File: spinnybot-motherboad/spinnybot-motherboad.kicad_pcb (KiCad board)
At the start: 2 copper layers, 76.2 x 76 mm, 55 parts, among them J1 +12V, J11 POWER SW2, J12 LEDSTRIP3, J13 LEDSTRIP2, J14 LEDSTRIP3, J2 LEDSTRIP1, J3 LEDSTRIP1, J4 LEDSTRIP2, J5 GND, J6 MOTOR2, J7 MOTOR3, J8 MOTOR1, J9 POWER SW1, Q1 SISA96DN, Q2 SISA96DN, Q3 BC846, Q4 Q_NMOS_DGS, U1 LM1117-3.3, U2 XBP9B-DMWTB002, U4 ICM-20649, U5 ESP32-DEVKITC-32D, U6 SN74AHCT541DW, U7 SN74AHCT541DW

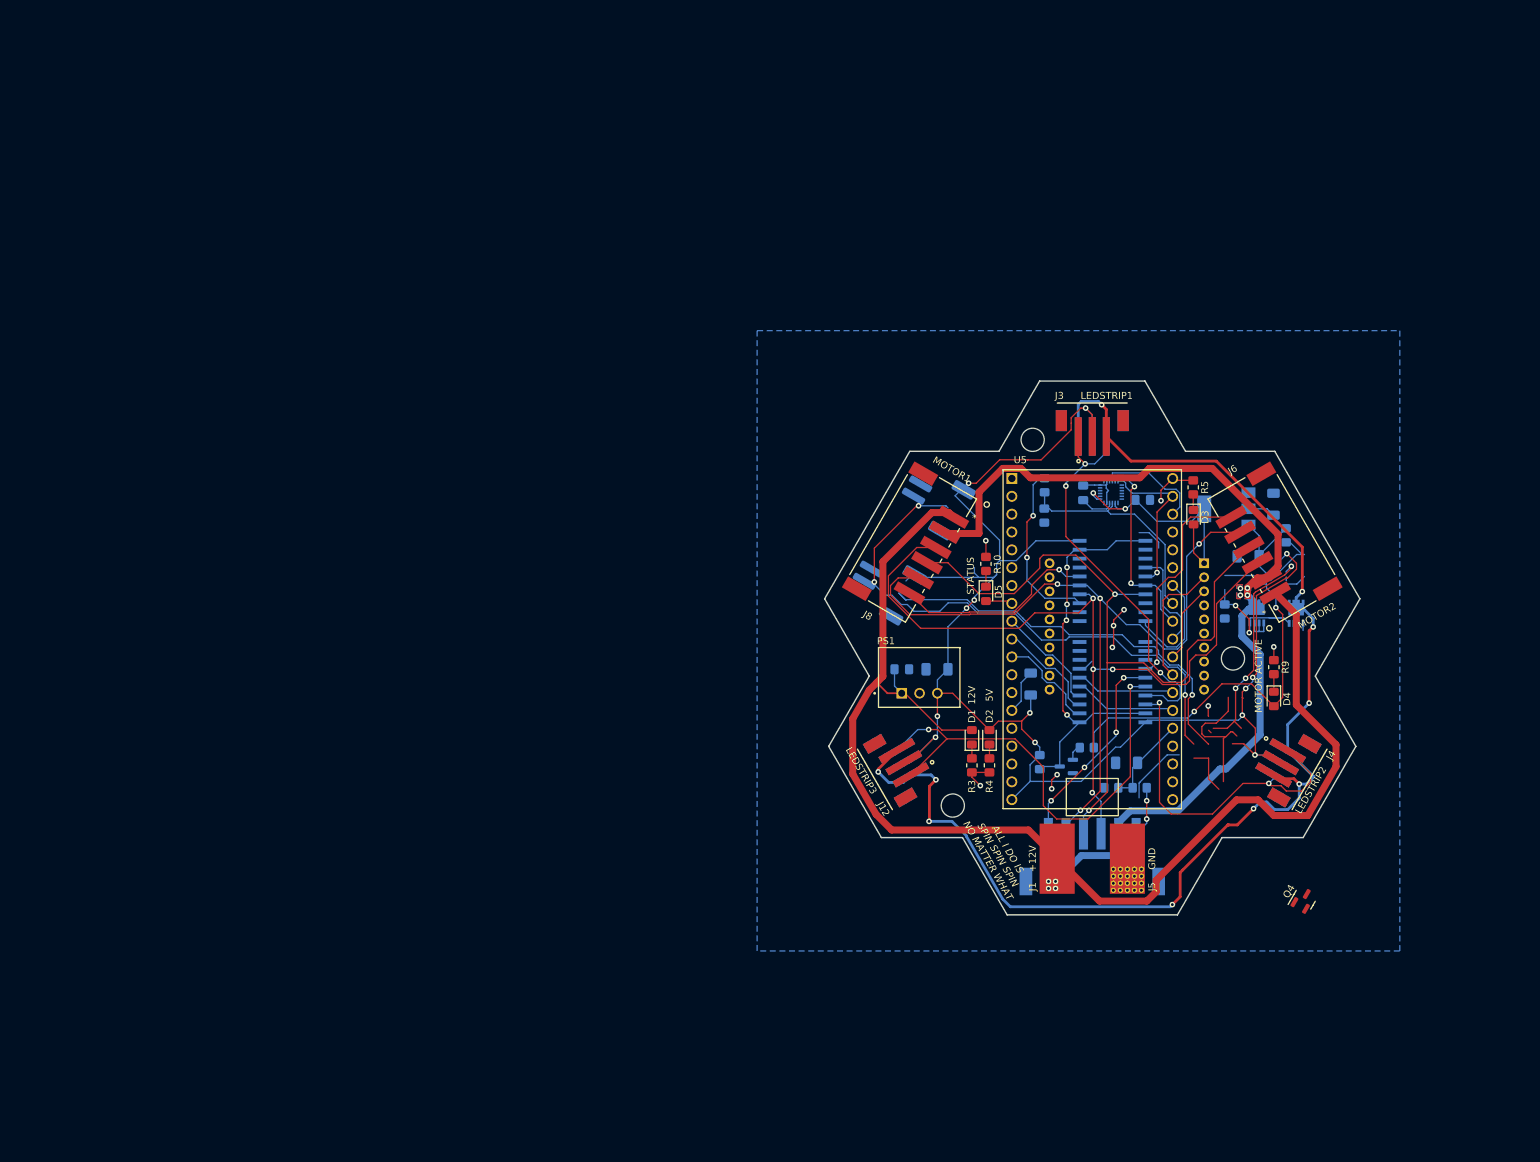
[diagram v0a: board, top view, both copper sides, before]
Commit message: Started board layout
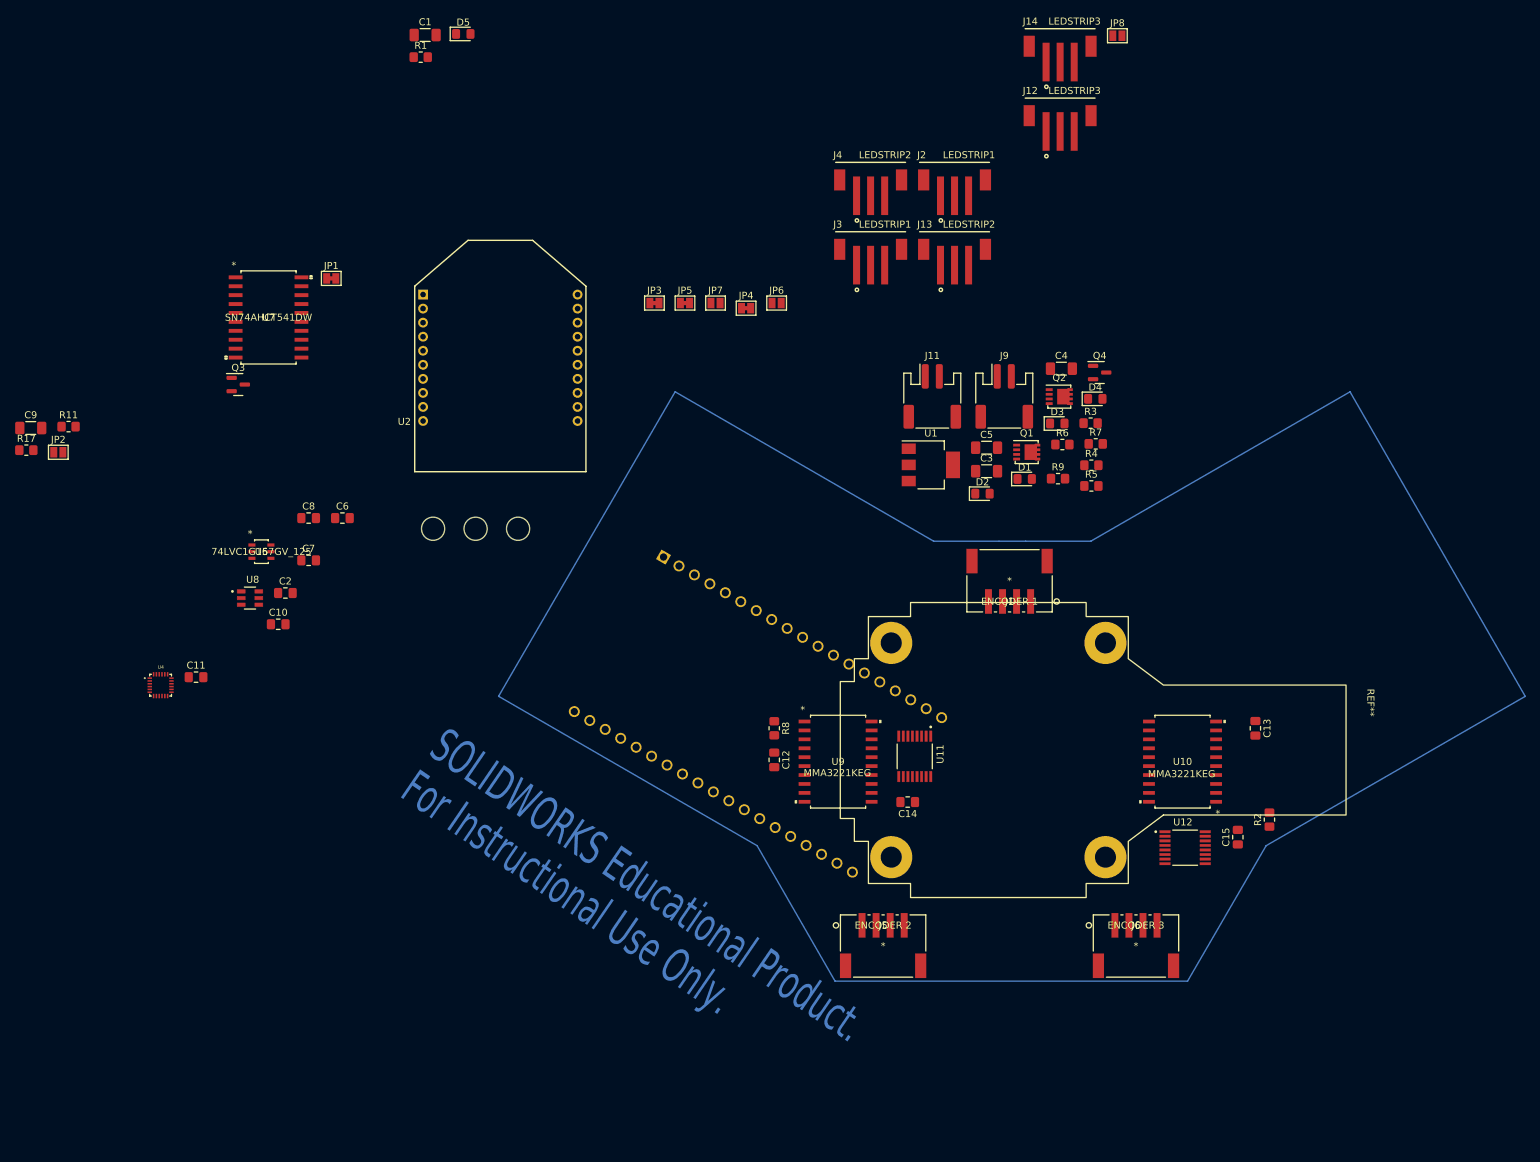
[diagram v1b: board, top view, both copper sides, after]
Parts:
- removed #LOGO1: LOGO, robologo-shenzen-25mm:F.SilkS_g1611
- removed #LOGO2: nofcc, robologo-shenzen-25mm:nofcc
- removed J7: MOTOR3, S6B-XH-SM4-TB:S6B-XH-SM4-TBLFSN
- removed J8: MOTOR1, S6B-XH-SM4-TB:S6B-XH-SM4-TBLFSN
- removed PS1: R-78E5.0-1.0, R-78E5:CONV_R-78E5.0-1.0
- removed R10: 130, Resistor_SMD:R_0805_2012Metric_Pad1.20x1.40mm_HandSolder
- removed R12: 1K, Resistor_SMD:R_0805_2012Metric_Pad1.20x1.40mm_HandSolder
- removed R13: 2K, Resistor_SMD:R_0805_2012Metric_Pad1.20x1.40mm_HandSolder
- added C10: 0.1u, Capacitor_SMD:C_0805_2012Metric_Pad1.18x1.45mm_HandSolder, F.Cu at (56.9, 99.2)
- added C11: 0.1u, Capacitor_SMD:C_0805_2012Metric_Pad1.18x1.45mm_HandSolder, F.Cu at (45.2, 106.7)
- added C12: 0.1u, Capacitor_SMD:C_0805_2012Metric_Pad1.18x1.45mm_HandSolder, F.Cu at (127.5, 118.5)
- added C13: 0.1u, Capacitor_SMD:C_0805_2012Metric_Pad1.18x1.45mm_HandSolder, F.Cu at (196.0, 114.0)
- added C14: 0.1u, Capacitor_SMD:C_0805_2012Metric_Pad1.18x1.45mm_HandSolder, F.Cu at (146.5, 124.5)
- added C15: 0.1u, Capacitor_SMD:C_0805_2012Metric_Pad1.18x1.45mm_HandSolder, F.Cu at (193.5, 129.5)
- added C6: 0.1u, Capacitor_SMD:C_0805_2012Metric_Pad1.18x1.45mm_HandSolder, F.Cu at (66.0, 84.1)
- added JP1: SolderJumper_2_Bridged, Jumper:SolderJumper-2_P1.3mm_Bridged_Pad1.0x1.5mm, F.Cu at (64.4, 50.0)
- added JP2: SolderJumper_2_Open, Jumper:SolderJumper-2_P1.3mm_Open_Pad1.0x1.5mm, F.Cu at (25.6, 74.7)
- added JP3: SolderJumper_2_Bridged, Jumper:SolderJumper-2_P1.3mm_Bridged_Pad1.0x1.5mm, F.Cu at (110.4, 53.5)
- added JP4: SolderJumper_2_Bridged, Jumper:SolderJumper-2_P1.3mm_Bridged_Pad1.0x1.5mm, F.Cu at (123.5, 54.2)
- added JP5: SolderJumper_2_Bridged, Jumper:SolderJumper-2_P1.3mm_Bridged_Pad1.0x1.5mm, F.Cu at (114.8, 53.5)
- added JP6: SolderJumper_2_Open, Jumper:SolderJumper-2_P1.3mm_Open_Pad1.0x1.5mm, F.Cu at (127.8, 53.5)
- added JP7: SolderJumper_2_Open, Jumper:SolderJumper-2_P1.3mm_Open_Pad1.0x1.5mm, F.Cu at (119.1, 53.5)
- added JP8: SolderJumper_2_Open, Jumper:SolderJumper-2_P1.3mm_Open_Pad1.0x1.5mm, F.Cu at (176.3, 15.4)
- added R8: 10k, Resistor_SMD:R_0805_2012Metric_Pad1.20x1.40mm_HandSolder, F.Cu at (127.5, 114.0)
- added REF**: ESC_Hobbywing_X-Rotor_Micro_60A_4in1, esc_4in1:ESC_Hobbywing_X-Rotor_Micro_60A_4in1, F.Cu at (208.9, 96.1)
- added U10: MMA3221KEG, MMA3221KEG:MMA3221KEG, F.Cu at (185.6, 118.8)
- added U11: ADS122U04IPWR, ADS122U04IPWR:SOP65P640X120-16N, F.Cu at (147.5, 118.0)
- added U12: ADS122U04IPWR, ADS122U04IPWR:SOP65P640X120-16N, F.Cu at (186.0, 131.0)
- added U8: SN74LVC1G18DBVR, SN74LVC1G18DBVR:SOT95P280X145-6N, F.Cu at (52.9, 95.5)
- added U9: MMA3221KEG, MMA3221KEG:MMA3221KEG, F.Cu at (136.6, 118.8)
- C1, C3, C4, C5, C7, C8, C9, J11, J13, J14, J2, J9, Q1, Q2, Q3, R11, R17, R6, U1, U2, U4, U7: moved to F.Cu
- C2: value 10u -> 0.1u; moved to F.Cu
- J1: value +12V -> ENCODER 1; footprint Connector_Wire:SolderWirePad_1x01_SMD_5x10mm -> S4B-PH-SM4-TB:S4B-PH-SM4-TBLFSN
- J5: value GND -> ENCODER 2; footprint custom:Stitched_SolderWirePad_1x01_SMD_5x10mm -> S4B-PH-SM4-TB:S4B-PH-SM4-TBLFSN
- J6: value MOTOR2 -> ENCODER 3; footprint S6B-XH-SM4-TB:S6B-XH-SM4-TBLFSN -> S4B-PH-SM4-TB:S4B-PH-SM4-TBLFSN
- R1: value 3.92K -> 130; moved to F.Cu
- R2: value 909 -> 10k; moved to F.Cu
- R7: value 2k -> 150k; moved to F.Cu
- U5: footprint NODEMCU_ESP32:MODULE_NODEMCU_ESP32 -> esp32-devkitc-32d:MODULE_ESP32-DEVKITC-32D; moved to B.Cu
- U6: value SN74AHCT541DW -> 74LVC1G157GV_125; footprint SN74AHCT541DW:SN74AHCT541DW -> 74LVC1G157GV,125:74LVC1G157GV_125; moved to F.Cu
- moved R17 156.8 mm to (21.0, 74.4)
- moved C9 147.0 mm to (21.6, 71.2), turned to 0 degrees
- moved R11 146.3 mm to (27.0, 71.0), turned to 0 degrees
- moved R1 145.9 mm to (77.2, 18.4), turned to 0 degrees
- moved C1 143.9 mm to (77.8, 15.3), turned to 0 degrees
- moved U4 138.1 mm to (40.1, 107.9), turned to 0 degrees
- moved U7 130.9 mm to (55.5, 55.5)
- moved Q3 129.8 mm to (51.2, 65.1), turned to 0 degrees
- moved U6 121.2 mm to (54.5, 88.9), turned to 0 degrees
- moved C8 118.8 mm to (61.2, 84.1)
- moved C7 110.7 mm to (61.2, 90.1), turned to 0 degrees
- moved H4 109.4 mm to (85.0, 85.6)
- moved D5 109.1 mm to (83.2, 15.1), turned to 0 degrees
- moved J14 105.9 mm to (168.2, 16.9), turned to 0 degrees
- moved J4 103.5 mm to (141.2, 35.9), turned to 0 degrees
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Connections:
- net /MCU and Buffers/IMU_CS renamed /IMU_CS
- net /MCU and Buffers/MISO_3V3 renamed /MISO_3V3
- C1 pad 1: /12V_SENSE -> +3V3
- C2 pad 1: GND -> +3V3
- C2 pad 2: +12V -> GND
- J1 pad 1: +12V -> /ENC_1A_5V
- J5 pad 1: GND -> /ENC_2A_5V
- J6 pad 1: +12V -> /ENC_3A_5V
- J6 pad 2: /MOTOR_NEG -> /ENC_3B_5V
- J6 pad 3: /SCK_5V -> GND
- J6 pad 4: /MISO_5V -> +5V
- J6 pad 5: /MOSI_5V -> (no net)
- J6 pad 6: /MOTOR_CS2_5V -> (no net)
- Q2 pad 5: /MOTOR_NEG -> /ESC_GND
- R1 pad 1: +12V -> GND
- R1 pad 2: /12V_SENSE -> Net-(D5-Pad1)
- R2 pad 1: /12V_SENSE -> /ACCEL_SELF_TEST
- U4 pad 23: /MCU and Buffers/SCK_3V3 -> /SCK_3V3
- U4 pad 24: /MCU and Buffers/MOSI_3V3 -> /MOSI_3V3
- U5 pad 12: unconnected-(U5-Pad12) -> /MCU and Buffers/ENC_1A_3V3
- U5 pad 13: unconnected-(U5-Pad13) -> /MCU and Buffers/ENC_1B_3V3
- U5 pad 15: unconnected-(U5-Pad15) -> /ADC_SEL
- U5 pad 16: unconnected-(U5-Pad16) -> /ADC_TX
- U5 pad 17: unconnected-(U5-Pad17) -> /ADC_RX
- U5 pad 21: /MCU and Buffers/MOSI_3V3 -> /MOSI_3V3
- U5 pad 25: unconnected-(U5-Pad25) -> /MCU and Buffers/LEDSTRIP3_DATA_3V3
- U5 pad 28: /MCU and Buffers/SCK_3V3 -> /SCK_3V3
- U5 pad 29: /MCU and Buffers/MOTOR_CS1_3V3 -> Net-(D5-Pad2)
- U5 pad 32: /MCU and Buffers/MOTOR_CS2_3V3 -> /MCU and Buffers/ENC_2A_3V3
- U5 pad 33: /MCU and Buffers/MOTOR_CS3_3V3 -> /MCU and Buffers/ENC_2B_3V3
- U5 pad 34: /12V_SENSE -> /MCU and Buffers/ENC_3A_3V3
- U5 pad 35: unconnected-(U5-Pad35) -> /MCU and Buffers/ENC_3B_3V3
- U5 pad 7: unconnected-(U5-Pad7) -> /ESC_S1
- U5 pad 8: Net-(D5-Pad2) -> /ESC_S2
- U5 pad 9: /MCU and Buffers/LEDSTRIP3_DATA_3V3 -> /ESC_S3
- U6 pad 1: /MCU and Buffers/BUFFER_OE -> /IMU and Accelerometers/ADC2_RX
- U6 pad 3: GND -> /IMU and Accelerometers/ADC1_RX
- U6 pad 4: /MCU and Buffers/MOTOR_CS1_3V3 -> /ADC_RX
- U6 pad 5: /MCU and Buffers/MOSI_3V3 -> +3V3
- U6 pad 6: /MCU and Buffers/SCK_3V3 -> /ADC_SEL
- U7 pad 14: /MOTOR_CS2_5V -> unconnected-(U7-Pad14)
- U7 pad 15: /MOTOR_CS3_5V -> unconnected-(U7-Pad15)
- U7 pad 5: /MCU and Buffers/MOTOR_CS3_3V3 -> unconnected-(U7-Pad5)
- U7 pad 6: /MCU and Buffers/MOTOR_CS2_3V3 -> unconnected-(U7-Pad6)
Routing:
- net +5V: track 302.7 -> 0.00 mm, vias 15 -> 0
- net +12V: track 208.8 -> 0.00 mm, vias 6 -> 0
- net /LEDSTRIP_GND: track 182.8 -> 0.00 mm, vias 10 -> 0
- net /MOTOR_NEG: track 121.0 -> 0.00 mm, vias 4 -> 0
- net /SCK_5V: track 116.9 -> 0.00 mm, vias 4 -> 0
- net (no net): track 112.8 -> 0.00 mm, vias 4 -> 0
- net /MOSI_5V: track 111.7 -> 0.00 mm, vias 4 -> 0
- net /MISO_5V: track 110.3 -> 0.00 mm, vias 2 -> 0
- net Net-(J11-Pad2): track 89.9 -> 0.00 mm, vias 3 -> 0
- net GND: track 87.9 -> 0.00 mm, vias 10 -> 0
- net /LEDSTRIP3_DATA_5V: track 67.7 -> 0.00 mm, vias 2 -> 0
- net /MCU and Buffers/BUFFER_OE: track 57.6 -> 0.00 mm, vias 4 -> 0
- net /LEDSTRIP1_DATA_5V: track 57.4 -> 0.00 mm, vias 3 -> 0
- net /LEDSTRIP2_DATA_5V: track 48.6 -> 0.00 mm, vias 2 -> 0
- net +3V3: track 40.7 -> 0.00 mm, vias 2 -> 0
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- removed copper zone on B.Cu, net /MOTOR_NEG
- removed copper zone on F.Cu, net /MOTOR_NEG
- removed copper zone on B.Cu, net GND
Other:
- board outline removed
- board text added: "For Instructional Use Only."
- board text added: "SOLIDWORKS Educational Product."
- board text removed: "ALL I DO IS SPIN SPIN SPIN NO MATTER WHAT"
- board text removed: "SPINNYBOT MOTHERBOARD REV2 DUSTIN RICHARDS ROCKERBOTICS 2021 SOUTH DAKOTA MINES"

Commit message: Continued adding to board layout, added missing ESC connector footprint
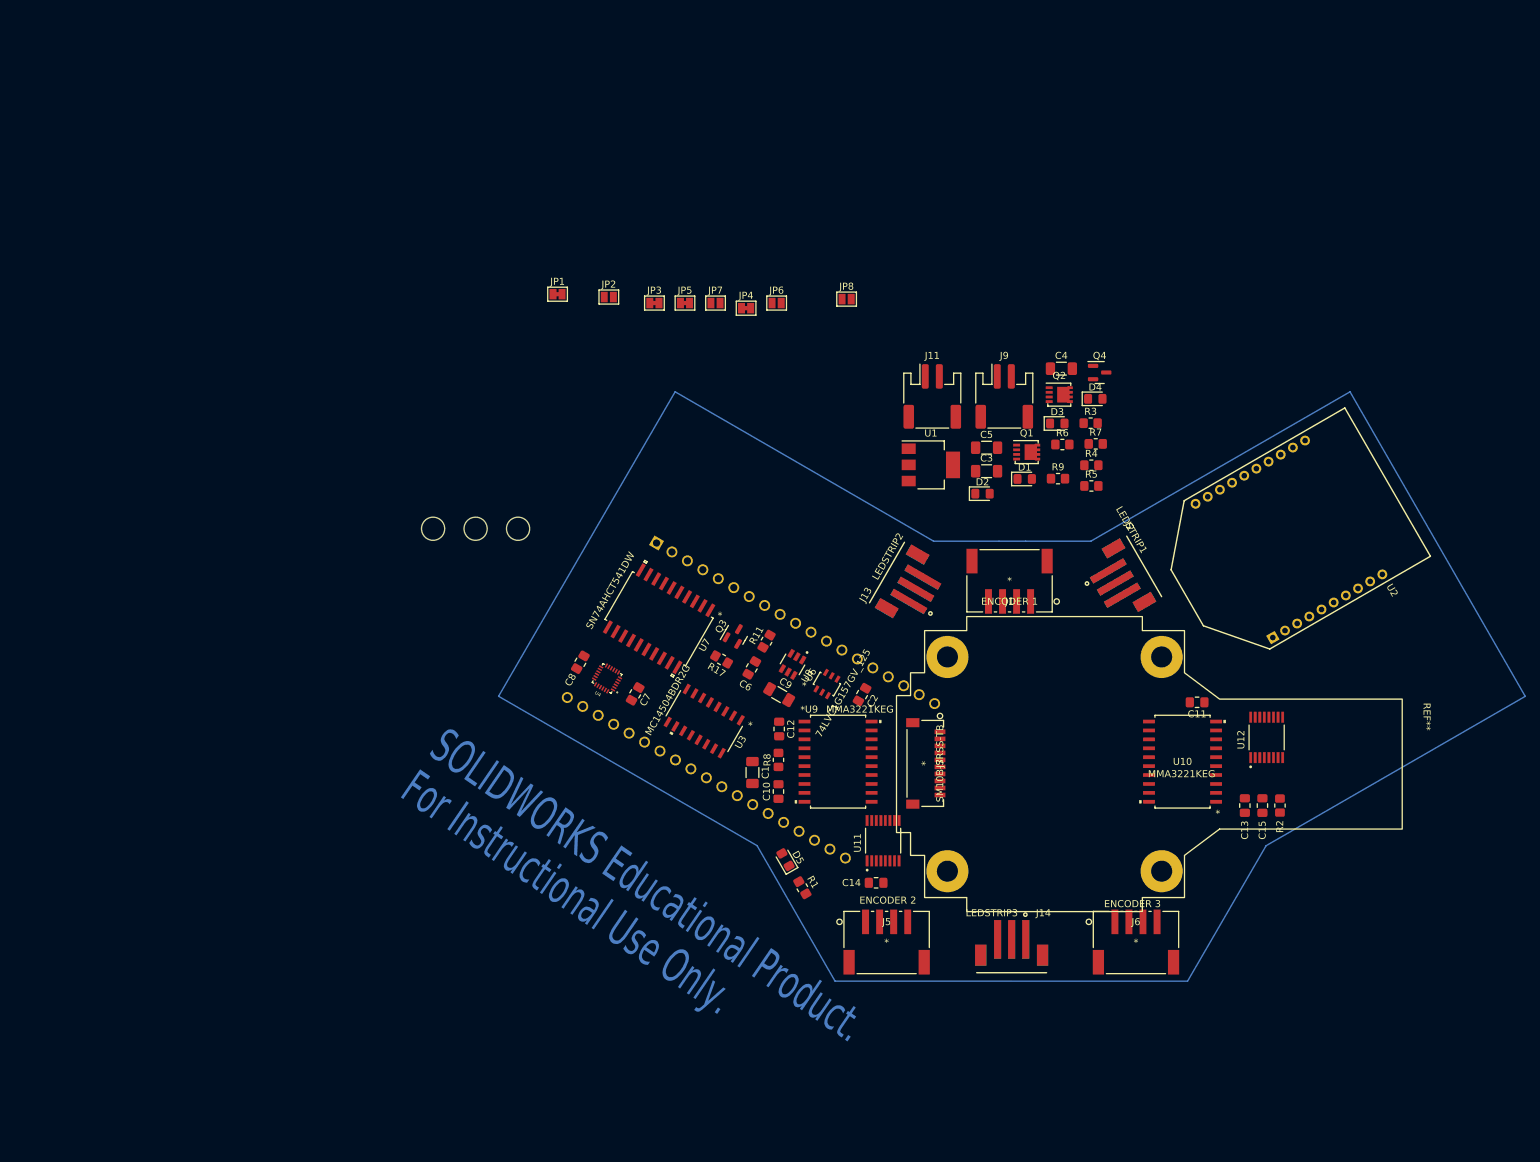
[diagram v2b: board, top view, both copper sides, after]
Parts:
- added J7: SM10B-SRSS-TB, esc_4in1:SM10B-SRSS-TB, F.Cu at (149.0, 119.0)
- added U3: MC14504BDR2G, MC14504BDR2G:MC14504BDR2G, F.Cu at (117.5, 113.0)
- J12, J3, J4: moved to B.Cu
- moved C11 142.6 mm to (187.7, 110.3), turned to 180 degrees
- moved R1 130.1 mm to (131.5, 136.7), turned to 120 degrees
- moved J14 129.6 mm to (161.3, 146.3), turned to 180 degrees
- moved D5 126.2 mm to (129.1, 132.7), turned to 120 degrees
- moved J12 119.7 mm to (161.3, 146.3)
- moved U2 115.1 mm to (200.6, 87.2), turned to 120 degrees
- moved C1 114.9 mm to (124.4, 120.3), turned to -90 degrees
- moved C9 113.1 mm to (128.2, 109.2), turned to -30 degrees
- moved R11 104.0 mm to (126.4, 101.6), turned to 60 degrees
- moved R17 103.4 mm to (120.0, 104.2), turned to -30 degrees
- moved C2 83.4 mm to (140.0, 109.2), turned to -120 degrees
- moved U6 82.7 mm to (135.0, 107.7), turned to 60 degrees
- moved JP2 81.4 mm to (104.0, 52.6)
- moved Q3 79.3 mm to (122.0, 100.7), turned to 60 degrees
- moved U8 77.8 mm to (130.1, 104.9), turned to -120 degrees
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
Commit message: Most of the parts on the board, still missing battery connections
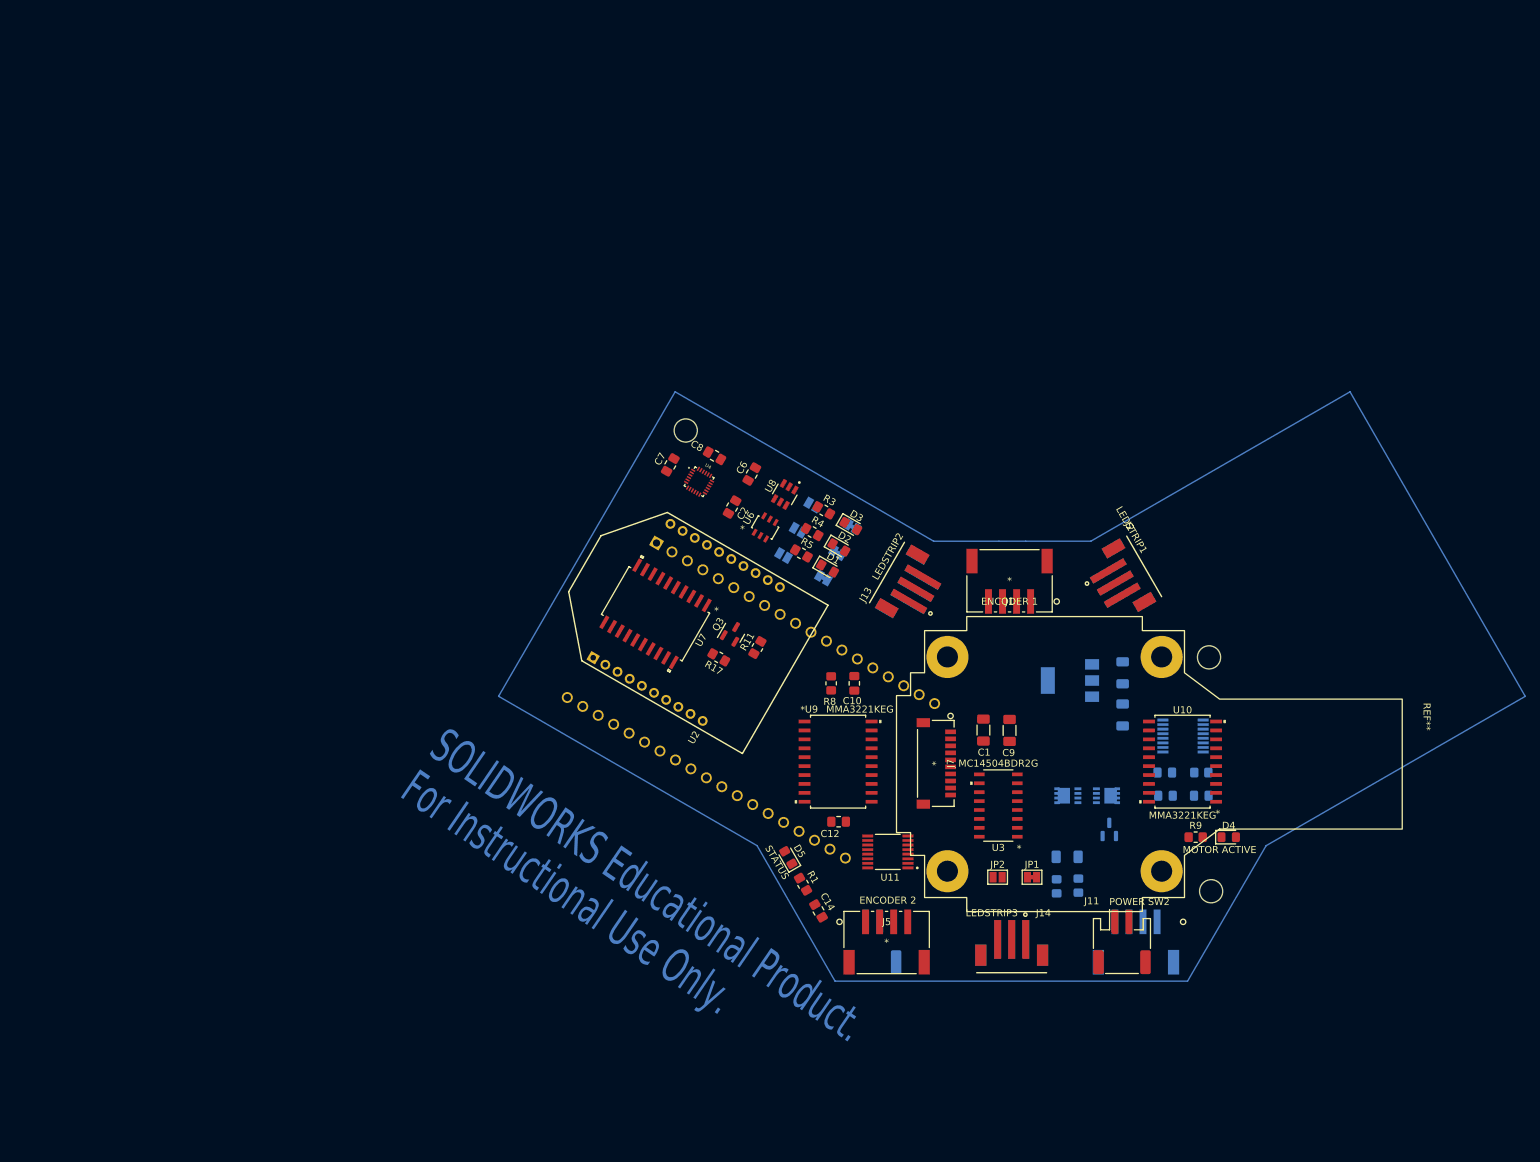
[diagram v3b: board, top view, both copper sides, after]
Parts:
- C11, C13, C15, C3, C4, C5, J6, J9, JP3, JP4, JP5, JP6, JP7, JP8, Q1, Q2, Q4, R2, R6, R7, U1, U12: moved to B.Cu
- moved H1 122.2 mm to (189.7, 137.2)
- moved JP1 107.0 mm to (164.2, 135.2)
- moved H4 106.0 mm to (189.4, 103.9)
- moved JP2 99.4 mm to (159.3, 135.2)
- moved U2 86.5 mm to (114.8, 98.8), turned to 60 degrees
- moved J11 82.2 mm to (177.0, 144.4)
- moved J9 79.9 mm to (141.5, 144.4), turned to 180 degrees
- moved D4 65.2 mm to (192.2, 129.5)
- moved Q4 65.1 mm to (175.2, 128.4), turned to 90 degrees
- moved R7 62.9 mm to (170.8, 136.4), turned to 90 degrees
- moved R6 62.9 mm to (167.7, 136.5), turned to -90 degrees
- moved C5 59.4 mm to (169.2, 132.3)
- moved Q2 57.5 mm to (174.8, 123.6)
- moved R9 54.7 mm to (187.5, 129.5)
- moved Q1 49.3 mm to (169.3, 123.6), turned to 180 degrees
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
